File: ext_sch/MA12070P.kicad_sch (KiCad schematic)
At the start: 49 parts

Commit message: Updated readme and pictures!
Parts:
- C12, C13, C14, C15, C31, C32, C34, C35: value (none) -> 10uF; footprint (none) -> Capacitor_SMD:C_0805_2012Metric
- C16, C19, C21, C22, C23, C24, C26: value (none) -> 1uF; footprint (none) -> Capacitor_SMD:C_0603_1608Metric
- C17, C18, C27, C29, C33: value (none) -> 100nF; footprint (none) -> Capacitor_SMD:C_0603_1608Metric
- C20, C25, C28, C30: value (none) -> 1uF; footprint (none) -> Capacitor_SMD:C_0805_2012Metric
- C36, C37, C38, C39: value (none) -> 150uF; footprint (none) -> Capacitor_SMD:CP_Elec_8x10
- C40, C41, C42, C43: value (none) -> 1nF; footprint (none) -> Capacitor_SMD:C_0603_1608Metric
- C44, C45: value (none) -> 22nF; footprint (none) -> Capacitor_SMD:C_0603_1608Metric
- FB1, FB2, FB3, FB4: value (none) -> Ferrite_Bead; footprint (none) -> Capacitor_SMD:C_1206_3216Metric
- J6, J7: value (none) -> Screw Term.; footprint (none) -> Lib:Phoenix1989447
- JP3, JP4: value (none) -> Jumper_3_Bridged; footprint (none) -> Jumper:SolderJumper-3_P1.3mm_Bridged12_RoundedPad1.0x1.5mm
- L2: value (none) -> MA_Ferrite; footprint (none) -> Lib:MA_Ferrite
- R26: value (none) -> 100KΩ; footprint (none) -> Resistor_SMD:R_0603_1608Metric
- TP14, TP15, TP16, TP17: value (none) -> TestPoint_Small; footprint (none) -> TestPoint:TestPoint_Pad_D1.5mm
- U6: value (none) -> MA12070P; footprint (none) -> Package_DFN_QFN:QFN-64-1EP_9x9mm_P0.5mm_EP5.45x5.45mm_ThermalVias
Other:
- moved on the sheet: C12, C13, C14, C15, C16, C17, C18, C19, C20, C21, C22, C23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

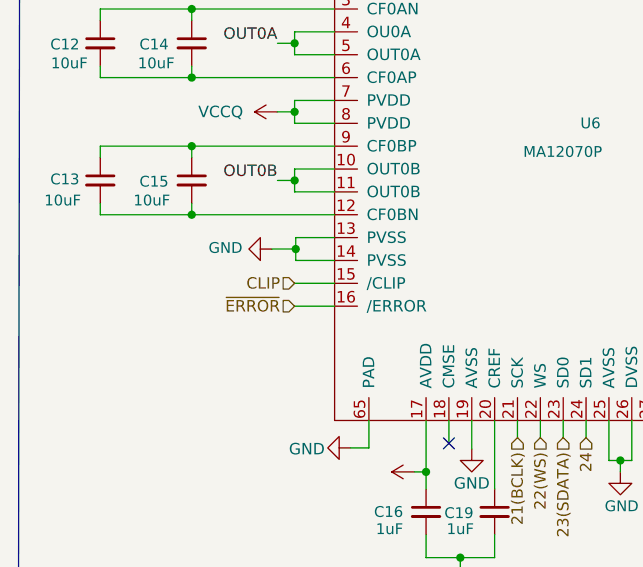
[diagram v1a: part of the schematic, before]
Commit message: Redid symbol value and footprints for DC_Prot. Dont relink sub-schematics i guess..
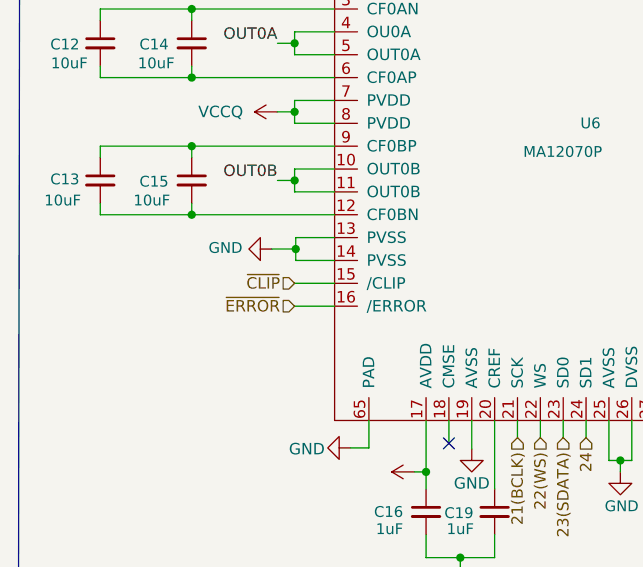
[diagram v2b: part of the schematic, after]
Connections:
- net CLIP renamed ~{CLIP}
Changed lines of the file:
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@@
     (effects (font (size 1.27 1.27)) (justify right))
   )
-  (hierarchical_label "CLIP" (shape input) (at 47.244 96.266 180)
+  (hierarchical_label "~{CLIP}" (shape input) (at 47.244 96.266 180)
     (effects (font (size 1.27 1.27)) (justify right))
   )

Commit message: Cleanup of schematic, and final gerbers
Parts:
- renumbered C28 to C16, C29 to C17, C16 to C18, C17 to C19, C18 to C20, C19 to C21, C20 to C22, C21 to C23, C30 to C24, C22 to C25, C33 to C26, C23 to C27, C24 to C28, C25 to C29, C26 to C30, C27 to C31, C36 to C32, C37 to C33, C38 to C34, C31 to C35, C32 to C36, C39 to C37, C34 to C38, C35 to C39, C44 to C40, C45 to C41, C40 to C42, C41 to C43, C42 to C44, C43 to C45

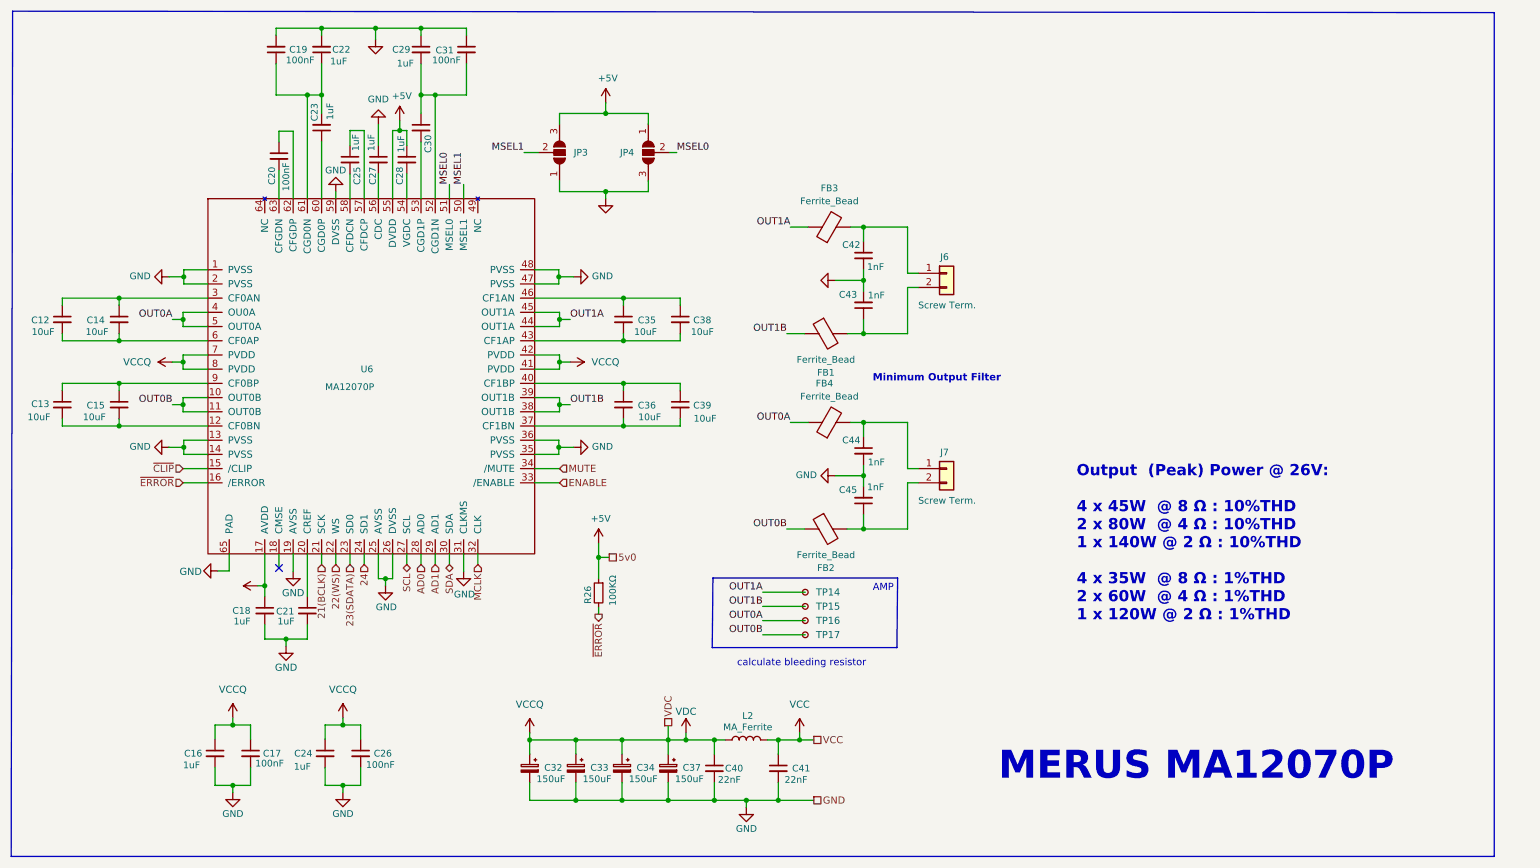
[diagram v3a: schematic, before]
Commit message: Latest revision: 3v3 LDO replaced with buck converter, 5v0 buck replaced, LED configuration changed, speaker terminals replaced with sping connector, and new audio pepriheral FPC connector added. Besides this all data traces have been rerouted, the board has been shortened about 8mm.
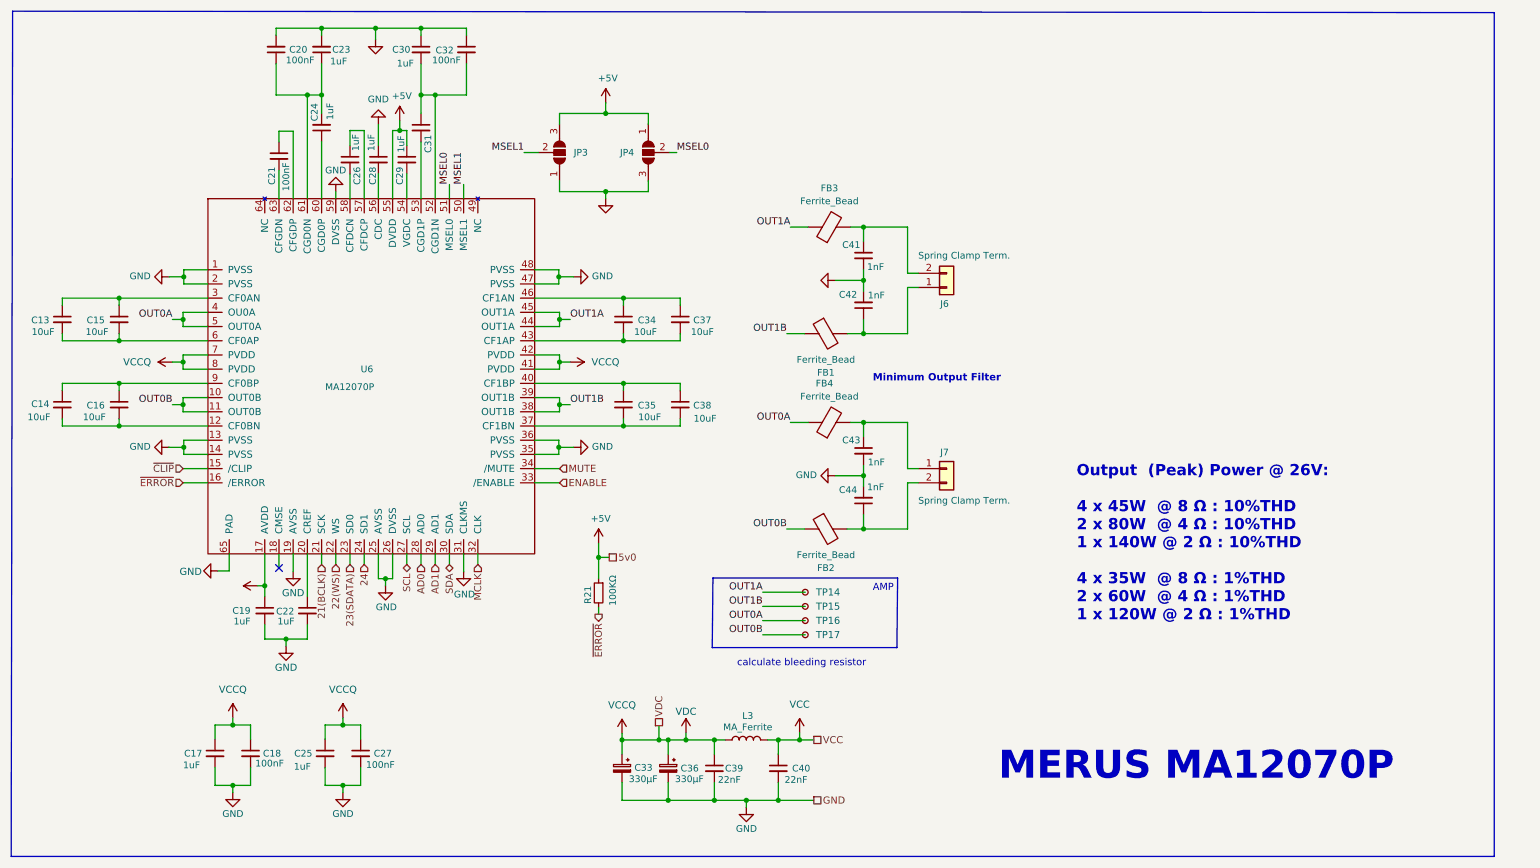
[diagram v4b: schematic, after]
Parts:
- removed C32, C34, C37: 150uF, Capacitor_SMD:CP_Elec_8x10, symbol Device:C_Polarized_Small
- added C36: 330µF, Capacitor_SMD:CP_Elec_10x10, symbol Device:C_Polarized_Small
- C33: value 150uF -> 330µF; footprint Capacitor_SMD:CP_Elec_8x10 -> Capacitor_SMD:CP_Elec_10x10; LCSC C38513 -> C280411
- J6, J7: value Screw Term. -> Spring Clamp Term.; footprint Lib:Phoenix1989447 -> Lib:Cixi Kefa Sping 2Pin; Digikey 277-16667-ND -> C475154
- renumbered C12 to C13, C13 to C14, C14 to C15, C15 to C16, C16 to C17, C17 to C18, C18 to C19, C19 to C20, C20 to C21, C21 to C22, C22 to C23, C23 to C24, C24 to C25, C25 to C26, C26 to C27, C27 to C28, C28 to C29, C29 to C30, C30 to C31, C31 to C32, C35 to C34, C36 to C35, C38 to C37, C39 to C38, C40 to C39, C41 to C40, C42 to C41, C43 to C42, C44 to C43, C45 to C44, L2 to L3, R26 to R21
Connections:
- net GND: now also C36.2
- net VCCQ: now also C36.1
- net at C42.1, FB1.2: now also J6.1 (Pin_1); no longer J6.2 (Pin_2)
- net at C41.1, FB3.2: now also J6.2 (Pin_2); no longer J6.1 (Pin_1)
